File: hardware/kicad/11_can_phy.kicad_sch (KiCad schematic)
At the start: 12 parts, among them J1101 CAN, U1101 TJA1051T/3

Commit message: sem-motor-controller v0.3: vehicle-interface provenance, transport-neutral core, clock trees, schematic checks
Provenance: the Cornell repositories are reference projects. Every place
that treated CHUDS / CAN FD / its VCU / 40 MHz as our vehicle is relabelled
or corrected (docs/PROVENANCE_AUDIT.md); the v0.2 checkpoint is preserved
with an errata banner.

Firmware: the core is transport-neutral (mc_core_on_msg_rx /
mc_core_msg_tx_poll / mc_core_on_link_state). CAN is one binding
(src/transport/mc_can_binding.c) whose 64-identifier block base is the new
calibration parameter supervision.can_id_base (id 164, rule 40, null in the
unconfigured config). ADR-0012. Tests: block relocation with a full ECO
engagement at 0x500, neutral API, rule-40 C/Python parity.

Clocking: tools/clock_tree.py evaluates 28 complete clock trees x 4 bus
cases from ST register widths and HAL ranges; the v0.2 "40 MHz required"
claim is withdrawn and the crystal is unselected until the bus is known.

Schematic: INA228 pins renumbered (KiCad-library cross-check, secondary);
DRV8353S stays an explicit placeholder; crystal unselected; PWR_FLAGs added
after a new pin-type check (not an ERC) found 6 undriven-rail errors.
Real KiCad ERC not run (KiCad 7 has no CLI ERC; tools/run_kicad_erc.sh).

Telematics: combined architecture with the STM32U575 / CAN 2.0B / LTE-MQTT
proposal (supervisor and CSIA placement, torque-request and driver-
authorization paths, pit/cloud outside the control chain), interface
difference table, generated DBC, logging-capacity and auxiliary-power
budget. Validation language separates command ceilings, envelope ramp,
phase current and battery current. CSIA: component attribution and a
next-evaluation plan; frozen results unchanged, nothing re-run.

Verified on the host: ctest 6/6 (4,006 checks), pytest 199 passed,
ARM core build 0 warnings, generators current, KiCad connectivity 0
problems. Nothing on hardware.

Co-Authored-By: Claude Opus 5.5 <noreply@anthropic.com>
Claude-Ses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
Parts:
- J1101: Rating_basis Cornell CHUDS harness connector and pinout to be confirmed -> vehicle CAN harness connector, pinout and termination UNKNO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
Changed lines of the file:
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@@
     (effects (font (size 1.27 1.27)) (justify right))
   )
-  (symbol (lib_id "Interface_CAN_LIN:TJA1051T-3") (at 83.82000000000001 71.12 0) (unit 1)
-    (in_bom yes) (on_board yes)
-    (property "Reference" "U1101" (id 0) (at 83.82000000000001 66.04 0)
-      (effects (font (size 1.27 1.27)))
-    )
-    (property "Value" "TJA1051T/3" (id 1) (at 83.82000000000001 76.2 0)
-      (effects (font (size 1.27 1.27)))
-    )
-    (property "Footprint" "" (id 2) (at 83.82000000000001 71.12 0)
-      (effects (font (size 1.27 1.27)) hide)
-    )
-    (property "Datasheet" "" (id 3) (at 83.82000000000001 71.12 0)
-      (effects (font (size 1.27 1.27)) hide)
-    )
-    (property "Status" "CANDIDATE (alternate TCAN1042V, pin-compatible class - verify)" (id 4) (at 83.82000000000001 71.12 0)
-      (effects (font (size 1.27 1.27)) hide)
-    )
-    (property "MPN" "TJA1051T/3/1J" (id 5) (at 83.82000000000001 71.12 0)
+  (symbol (lib_id "Interface_CAN_LIN:TJA1051T-3") (at 83.82 71.12 0) (unit 1)
+    (in_bom yes) (on_board yes)
+    (property "Reference" "U1101" (id 0) (at 83.82 66.04 0)
+      (effects (font (size 1.27 1.27)))
+    )
+    (property "Value" "TJA1051T/3" (id 1) (at 83.82 76.2 0)
+      (effects (font (size 1.27 1.27)))
+    )
+    (property "Footprint" "" (id 2) (at 83.82 71.12 0)
+      (effects (font (size 1.27 1.27)) hide)
+    )
+    (property "Datasheet" "" (id 3) (at 83.82 71.12 0)
+      (effects (font (size 1.27 1.27)) hide)
+    )
+    (property "Status" "CANDIDATE (alternate TCAN1042V, pin-compatible class - verify)" (id 4) (at 83.82 71.12 0)
+      (effects (font (size 1.27 1.27)) hide)
+    )
+    (property "MPN" "TJA1051T/3/1J" (id 5) (at 83.82 71.12 0)
       (effects (font (size 1.27 1.27)) hide)
     )
@@
       (effects (font (size 1.27 1.27)) hide)
     )
-    (property "Rating_basis" "Cornell CHUDS harness connector and pinout to be confirmed" (id 5) (at 261.62 109.22 0)
-      (effects (font (size 1.27 1.27)) hide)
-    )
+    (property "Rating_basis" "vehicle CAN harness connector, pinout and termination UNKNOWN (telematics proposal: CANH, CANL, GND)" (id 5) (at 261.62 109.22 0)
+      (effects (font (size 1.27 1.27)) hide)
+    )

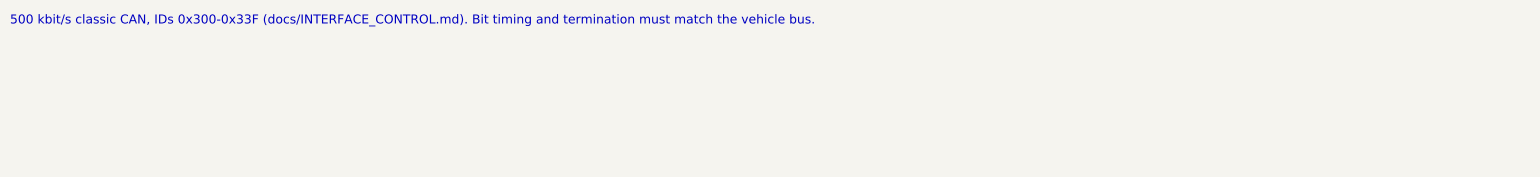
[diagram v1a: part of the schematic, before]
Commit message: repository tidy-up for the team: archive old records, plain status wording, CONTRIBUTING
Records of earlier releases (v0.1 handoff, v0.2 checkpoint, v0.3 review,
audits, the repository-move log, superseded interface and input sheets) move
to docs/archive/ with history kept; every link is updated and the archive has
its own README. The root now holds the README, CONTRIBUTING.md and the build
and test configuration only.

Statements about the tools' working environment ("unreachable from this
environment", network policy, proxy refusals) are replaced in the current
documents, tools and generated reports by plain project status: "datasheet
not yet read", "no supplier quote yet", "could not be accessed for this
work". Generated reports were regenerated, not edited; the CAN sheet note
now cites docs/ICD.md.

CONTRIBUTING.md: picking up work, branches and pull requests, who reviews
what, rules for engineering data, hardware safety, documentation. The
README opening points new members to it.

Full verification record replaced: verify_all --full in a fresh clone at
75f1b24, 37 PASS, 0 FAIL, 1 NOT AVAILABLE (KiCad ERC needs KiCad 8; it runs
in CI).

Co-Authored-By: Claude Opus 5.5 <noreply@anthropic.com>
Claude-Session: https://claude.ai/code/session_01GHmHZxA3w1n62SULRNT3dB
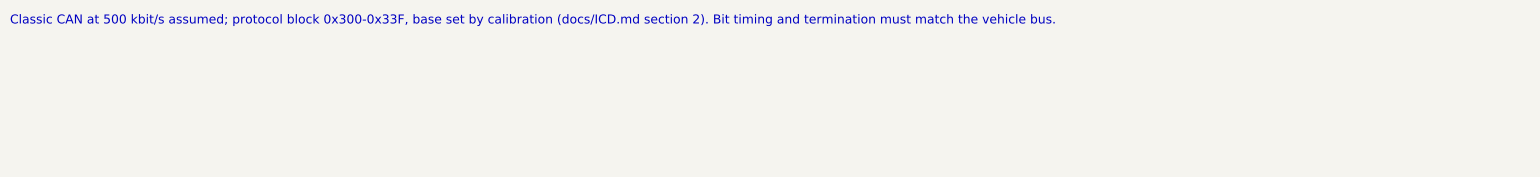
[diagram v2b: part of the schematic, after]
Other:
- note added: "Classic CAN at 500 kbit/s assumed; protocol block 0x300-0x33F, base set by calibration (docs/ICD.md section 2). Bit timing and termination must match the vehicle bus."
- note removed: "500 kbit/s classic CAN, IDs 0x300-0x33F (docs/INTERFACE_CONTROL.md). Bit timing and termination must match the vehicle bus."
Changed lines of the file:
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@@
     (comment 2 "Pin_check UNVERIFIED = pinout not checked against a primary datasheet")
   )
-  (text "500 kbit/s classic CAN, IDs 0x300-0x33F (docs/INTERFACE_CONTROL.md). Bit timing and termination must match the vehicle bus."
+  (text "Classic CAN at 500 kbit/s assumed; protocol block 0x300-0x33F, base set by calibration (docs/ICD.md section 2). Bit timing and termination must match the vehicle bus."
     (at 20.0 20.0 0)
     (effects (font (size 1.8 1.8)) (justify left))

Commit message: hardware: design review, OV comparator hysteresis fix, test points, KiCad 8.0.9 libraries
hardware/review/DESIGN_REVIEW.md reviews the draft item by item (gate
driver, MOSFETs, DC link, current sensing, hardware overcurrent,
over/undervoltage, temperature, precharge, enable defaults and
watchdog, emergency interface, DC-DC, CAN, clock, debug and test
points) with an evidence level per statement, and records what each
open item needs.

Schematic changes that need no vehicle data:
- the over-voltage comparator's hysteresis resistor went straight onto
  the TL431 node, whose low impedance made the hysteresis undefined;
  the + input is now fed through 10 k and 390 k from the output sets
  -2.5 % / +0.8 % around the reference;
- the TL431 bias is 470 ohm (1.7 mA) instead of 1 k (0.8 mA), above
  its minimum cathode current (recalled; to confirm in the datasheet);
- the six pull-downs on the gate-signal inputs are fitted until the
  driver's own pull-downs are verified;
- 21 test points for the signals the acceptance procedures probe.
Connectivity: 136 intended nets, 0 problems; pin types 0 findings;
consistency 14 PASS, 4 OPEN.

The nine KiCad 8.0.9 ERC warnings were each compared with the library:
PWR_FLAG pin name, TL431 drawing, STM32G474 symbol geometry and the
NUP2105L datasheet URL changed between the 7.0.11 library the
schematic embedded and 8.0.9; no pin number, connected name, type or
net changed. The schematic is now generated from a pinned, SHA-256
checked copy of the 8.0.9 libraries (tools/fetch_kicad_symbols.py),
which the ERC also reads; KiCad 8's (hide yes) spelling is converted
for kiutils so no field becomes visible. Both CI jobs use KiCad 8.

Firmware: the brake switch type is a calibration value; a separate
bench image (semmc_stm32g474_pwmtest) switches the gate signals at
fixed duties with DRV_ENABLE held low for acceptance stage 4; g_bench
also reports the input states.

Co-Authored-By: Claude Opus 5.5 <noreply@anthropic.com>
Claude-Session: https:/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
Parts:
- added TP1101: CAN_TX, symbol Connector:TestPoint
- added TP1102: CAN_RX, symbol Connector:TestPoint
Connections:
- net CAN_RX: now also TP1102.1
- net CAN_TX: now also TP1101.1
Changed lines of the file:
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@@
+    (effects (font (size 1.27 1.27)) (justify right))
+  )
+  (hierarchical_label "CAN_TX" (shape bidirectional) (at 378.46 106.68 270)
+    (effects (font (size 1.27 1.27)) (justify right))
+  )
+  (hierarchical_label "CAN_RX" (shape bidirectional) (at 436.88 106.68 270)
     (effects (font (size 1.27 1.27)) (justify right))
   )
@@
     (pin "2")
   )
+  (symbol (lib_id "Connector:TestPoint") (at 378.46 106.68 0) (unit 1)
+    (in_bom yes) (on_board yes)
+    (property "Reference" "TP1101" (id 0) (at 378.46 101.60000000000001 0)
+      (effects (font (size 1.27 1.27)))
+    )
+    (property "Value" "CAN_TX" (id 1) (at 378.46 111.76 0)
+      (effects (font (size 1.27 1.27)))
+    )
+    (property "Footprint" "" (id 2) (at 378.46 106.68 0)
+      (effects (font (size 1.27 1.27)) hide)
+    )
+    (property "Datasheet" "" (id 3) (at 378.46 106.68 0)
+      (effects (font (size 1.27 1.27)) hide)
+    )
+    (property "Status" "bench test point" (id 4) (at 378.46 106.68 0)
+      (effects (font (size 1.27 1.27)) hide)
+    )
+    (pin "1")
+  )
+  (symbol (lib_id "Connector:TestPoint") (at 436.88 106.68 0) (unit 1)
+    (in_bom yes) (on_board yes)
+    (property "Reference" "TP1102" (id 0) (at 436.88 101.60000000000001 0)
+      (effects (font (size 1.27 1.27)))
+    )
+    (property "Value" "CAN_RX" (id 1) (at 436.88 111.76 0)
+      (effects (font (size 1.27 1.27)))
+    )
+    (property "Footprint" "" (id 2) (at 436.88 106.68 0)
+      (effects (font (size 1.27 1.27)) hide)
+    )
+    (property "Datasheet" "" (id 3) (at 436.88 106.68 0)
+      (effects (font (size 1.27 1.27)) hide)
+    )
+    (property "Status" "bench test point" (id 4) (at 436.88 106.68 0)
+      (effects (font (size 1.27 1.27)) hide)
+    )
+    (pin "1")
+  )
   (sheet_instances

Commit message: hardware: footprint disposition for every BOM line, 82 assigned and checked
hardware/footprints/assignments.yaml gives each of the 122 BOM lines one
disposition. 68 lines are generic parts defined by value and package and
get a verified footprint (37 without the test points); 14 are specific
devices whose footprint is assigned from the KiCad 8.0.9 library but whose
manufacturer package drawing is unread (the LM5164 land pattern is drawn
from ST's L5973D HSOP-8 and the LQFP-100 from NXP's SOT407-1, so both must
be compared); 40 have none and say why: 28 rating-dependent, 4 waiting for a
data sheet value or pin voltage, 6 connectors, 2 placeholder pinouts.
Before this change no line had a footprint.

tools/check_footprints.py fetches the 25 footprint files used, pins them by
SHA-256, and checks per reference: numbered pads equal the symbol's pin
numbers, courtyard and fabrication outline present (copper-only jumpers and
net ties excepted), SMD or through-hole, package in the name for chip
parts, the symbol's footprint filters (as KiCad's ERC does), and pin 1 = K
on diode and LED symbols. Mutation tests cover a wrong pad count, a filter
miss, a package mismatch, a missing reference and a verified line without
a footprint. Small passives on battery-voltage nets (R104, R201, R202,
R1201) were kept rating-dependent rather than given an 0603.

The generator writes the footprints into the schematic and a footprint
column into the draft BOM; hw_consistency adds BM3 (netlist footprint
equals the BOM line's); price_bom takes footprint and package from the
assignment. Pricing rules fixed where lines matched the wrong rule: LEDs
were priced as buck inductors, crystal load capacitors as 100 V MLCCs, the
UART bench header as a harness connector, the reset switch and the Zener
under one generic rule; 22 uF and 4.7 uF now 1206 and 0805 for DC bias. One
board's parts move from $89-$239 to $88-$233. A project fp-lib-table and
the CI and ERC steps fetch the pinned footprints so the ERC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
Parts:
- C1101, C1102, C1103, C1104: footprint (none) -> Capacitor_SMD:C_0603_1608Metric
- D1101: footprint (none) -> Package_TO_SOT_SMD:SOT-23
- JP1101, JP1102: footprint (none) -> Jumper:SolderJumper-2_P1.3mm_Open_RoundedPad1.0x1.5mm
- R1101, R1102, R1103: footprint (none) -> Resistor_SMD:R_0603_1608Metric
- TP1101, TP1102: footprint (none) -> TestPoint:TestPoint_Pad_D1.5mm
- U1101: footprint (none) -> Package_SO:SOIC-8_3.9x4.9mm_P1.27mm
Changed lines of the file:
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@@
       (effects (font (size 1.27 1.27)))
     )
-    (property "Footprint" "" (id 2) (at 83.82 71.12 0)
+    (property "Footprint" "Package_SO:SOIC-8_3.9x4.9mm_P1.27mm" (id 2) (at 83.82 71.12 0)
       (effects (font (size 1.27 1.27)) hide)
     )
@@
       (effects (font (size 1.27 1.27)))
     )
-    (property "Footprint" "" (id 2) (at 154.94 66.04 0)
+    (property "Footprint" "Resistor_SMD:R_0603_1608Metric" (id 2) (at 154.94 66.04 0)
       (effects (font (size 1.27 1.27)) hide)
     )
@@
       (effects (font (size 1.27 1.27)))
     )
-    (property "Footprint" "" (id 2) (at 215.9 66.04 0)
+    (property "Footprint" "Capacitor_SMD:C_0603_1608Metric" (id 2) (at 215.9 66.04 0)
       (effects (font (size 1.27 1.27)) hide)
     )
@@
       (effects (font (size 1.27 1.27)))
     )
-    (property "Footprint" "" (id 2) (at 274.32 66.04 0)
+    (property "Footprint" "Capacitor_SMD:C_0603_1608Metric" (id 2) (at 274.32 66.04 0)
       (effects (font (size 1.27 1.27)) hide)
     )
@@
       (effects (font (size 1.27 1.27)))
     )
-    (property "Footprint" "" (id 2) (at 337.82 66.04 0)
+    (property "Footprint" "Package_TO_SOT_SMD:SOT-23" (id 2) (at 337.82 66.04 0)
       (effects (font (size 1.27 1.27)) hide)
     )
@@
       (effects (font (size 1.27 1.27)))
     )
-    (property "Footprint" "" (id 2) (at 403.86 60.96 0)
+    (property "Footprint" "Jumper:SolderJumper-2_P1.3mm_Open_RoundedPad1.0x1.5mm" (id 2) (at 403.86 60.96 0)
       (effects (font (size 1.27 1.27)) hide)
     )
@@
       (effects (font (size 1.27 1.27)))
     )
-    (property "Footprint" "" (id 2) (at 467.36 66.04 0)
+    (property "Footprint" "Resistor_SMD:R_0603_1608Metric" (id 2) (at 467.36 66.04 0)
       (effects (font (size 1.27 1.27)) hide)
     )
@@
       (effects (font (size 1.27 1.27)))
     )
-    (property "Footprint" "" (id 2) (at 71.12 111.76 0)
+    (property "Footprint" "Resistor_SMD:R_0603_1608Metric" (id 2) (at 71.12 111.76 0)
       (effects (font (size 1.27 1.27)) hide)
     )
@@
       (effects (font (size 1.27 1.27)))
     )
-    (property "Footprint" "" (id 2) (at 134.62 106.68 0)
+    (property "Footprint" "Jumper:SolderJumper-2_P1.3mm_Open_RoundedPad1.0x1.5mm" (id 2) (at 134.62 106.68 0)
       (effects (font (size 1.27 1.27)) hide)
     )
@@
       (effects (font (size 1.27 1.27)))
     )
-    (property "Footprint" "" (id 2) (at 198.12 111.76 0)
+    (property "Footprint" "Capacitor_SMD:C_0603_1608Metric" (id 2) (at 198.12 111.76 0)
       (effects (font (size 1.27 1.27)) hide)
     )
@@
       (effects (font (size 1.27 1.27)))
     )
-    (property "Footprint" "" (id 2) (at 317.5 111.76 0)
+    (property "Footprint" "Capacitor_SMD:C_0603_1608Metric" (id 2) (at 317.5 111.76 0)
       (effects (font (size 1.27 1.27)) hide)
     )
@@
       (effects (font (size 1.27 1.27)))
     )
-    (property "Footprint" "" (id 2) (at 378.46 106.68 0)
+    (property "Footprint" "TestPoint:TestPoint_Pad_D1.5mm" (id 2) (at 378.46 106.68 0)
       (effects (font (size 1.27 1.27)) hide)
     )
@@
       (effects (font (size 1.27 1.27)))
     )
-    (property "Footprint" "" (id 2) (at 436.88 106.68 0)
-      (effects (font (size 1.27 1.27)) hide)
-    )
+    (property "Footprint" "TestPoint:TestPoint_Pad_D1.5mm" (id 2) (at 436.88 106.68 0)
+      (effects (font (size 1.27 1.27)) hide)
+    )
